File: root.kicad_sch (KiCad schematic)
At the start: 0 parts

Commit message: MCU schematic
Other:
- sheet MCU renamed MCU (page 3)
- added sheet Peripherals (peripherals.kicad_sch)
- sheet MCU (page 3): file MCU.kicad_sch -> MCU_and_EEPROM.kicad_sch
- sheet MCU (page 3) ports: added USB_D_N, USB_D_P; removed none
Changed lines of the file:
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@@
 	(generator_version "10.0")
 	(paper "A4")
+	(wire
+		(pts
+			(xy 82.55 71.12) (xy 100.33 71.12)
+		)
+		(stroke
+			(width 0)
+			(type default)
+		)
+	)
+	(wire
+		(pts
+			(xy 82.55 73.66) (xy 100.33 73.66)
+		)
+		(stroke
+			(width 0)
+			(type default)
+		)
+	)
 	(sheet
 		(at 100.33 58.42)
@@
 			(color 0 0 0 0)
 		)
-		(property "Sheetname" "MCU"
+		(property "Sheetname" "MCU (page 3)"
 			(at 100.33 57.7084 0)
 			(show_name no)
@@
 			)
 		)
-		(property "Sheetfile" "MCU.kicad_sch"
+		(property "Sheetfile" "MCU_and_EEPROM.kicad_sch"
 			(at 100.33 92.0246 0)
 			(show_name no)
@@
 				)
 				(justify left top)
+			)
+		)
+		(pin "USB_D_N" bidirectional
+			(at 100.33 71.12 180)
+			(effects
+				(font
+					(size 1.27 1.27)
+				)
+				(justify left)
+			)
+		)
+		(pin "USB_D_P" bidirectional
+			(at 100.33 73.66 180)
+			(effects
+				(font
+					(size 1.27 1.27)
+				)
+				(justify left)
 			)
 		)
@@
 				)
 			)
+		)
+	)
+	(sheet
+		(at 100.33 19.05)
+		(size 41.91 29.21)
+		(exclude_from_sim no)
+		(in_bom yes)
+		(on_board yes)
+		(dnp no)
+		(fields_autoplaced yes)
+		(stroke
+			(width 0.1524)
+			(type solid)
+		)
+		(fill
+			(color 0 0 0 0)
+		)
+		(property "Sheetname" "Peripherals"
+			(at 100.33 18.3384 0)
+			(show_name no)
+			(do_not_autoplace no)
+			(effects
+				(font
+					(size 1.27 1.27)
+				)
+				(justify left bottom)
+			)
+		)
+		(property "Sheetfile" "peripherals.kicad_sch"
+			(at 100.33 48.8446 0)
+			(show_name no)
+			(do_not_autoplace no)
+			(effects
+				(font
+					(size 1.27 1.27)
+				)
+				(justify left top)
+			)
+		)
+		(instances
+			(project "octo_keyboard"
+				(path "/e2f6b5f5-4c68-42ad-a343-f16c1cb3ab86"
+					(page "6")
+				)
+			)

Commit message: peripherals finished
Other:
- sheet MCU (page 3): file MCU_and_EEPROM.kicad_sch -> MCU.kicad_sch
- sheet MCU (page 3) ports: added COL0, COL1, COL10, COL11, COL12, COL13, COL14, COL2, COL3, COL4, COL5, COL6, COL7, COL8, COL9, EEPROM_SCL, EEPROM_SDA, LED_DATA, ROW0, ROW1, ROW2, ROW3, ROW4, ROW5, SCREEN_CS, SCREEN_DS, SCREEN_SCL, SCREEN_SDA; removed none
- sheet Peripherals ports: added EEPROM_SCL, EEPROM_SDA; removed none

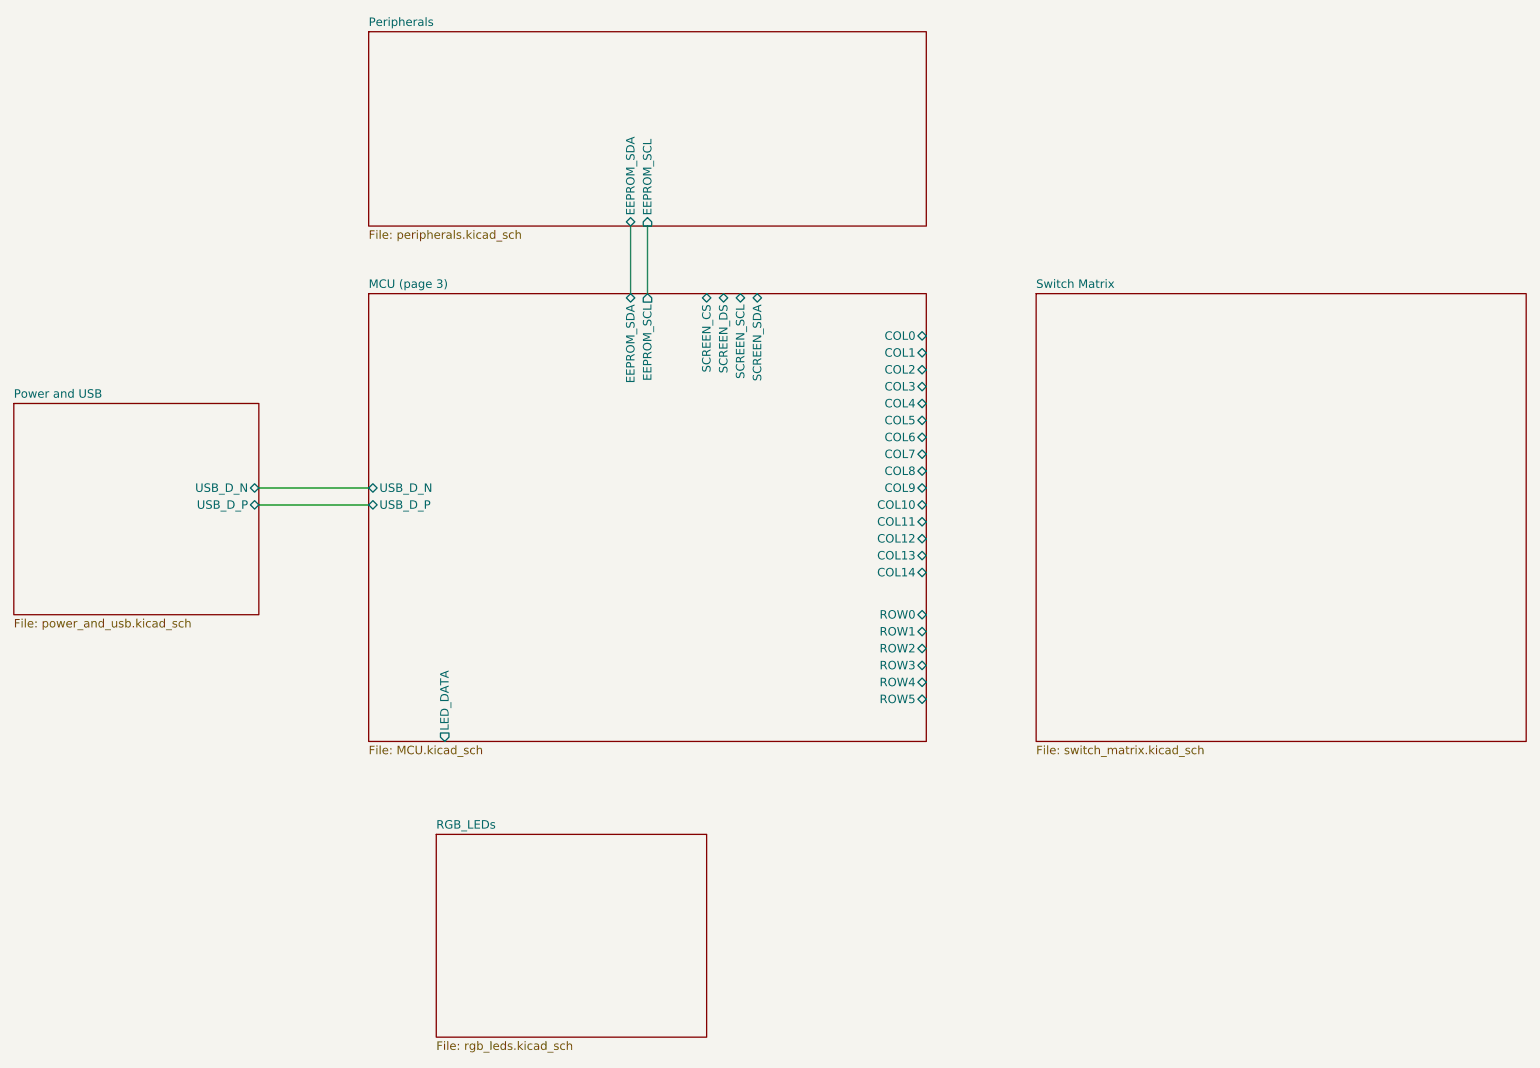
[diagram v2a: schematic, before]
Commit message: cleaned up top-level connections
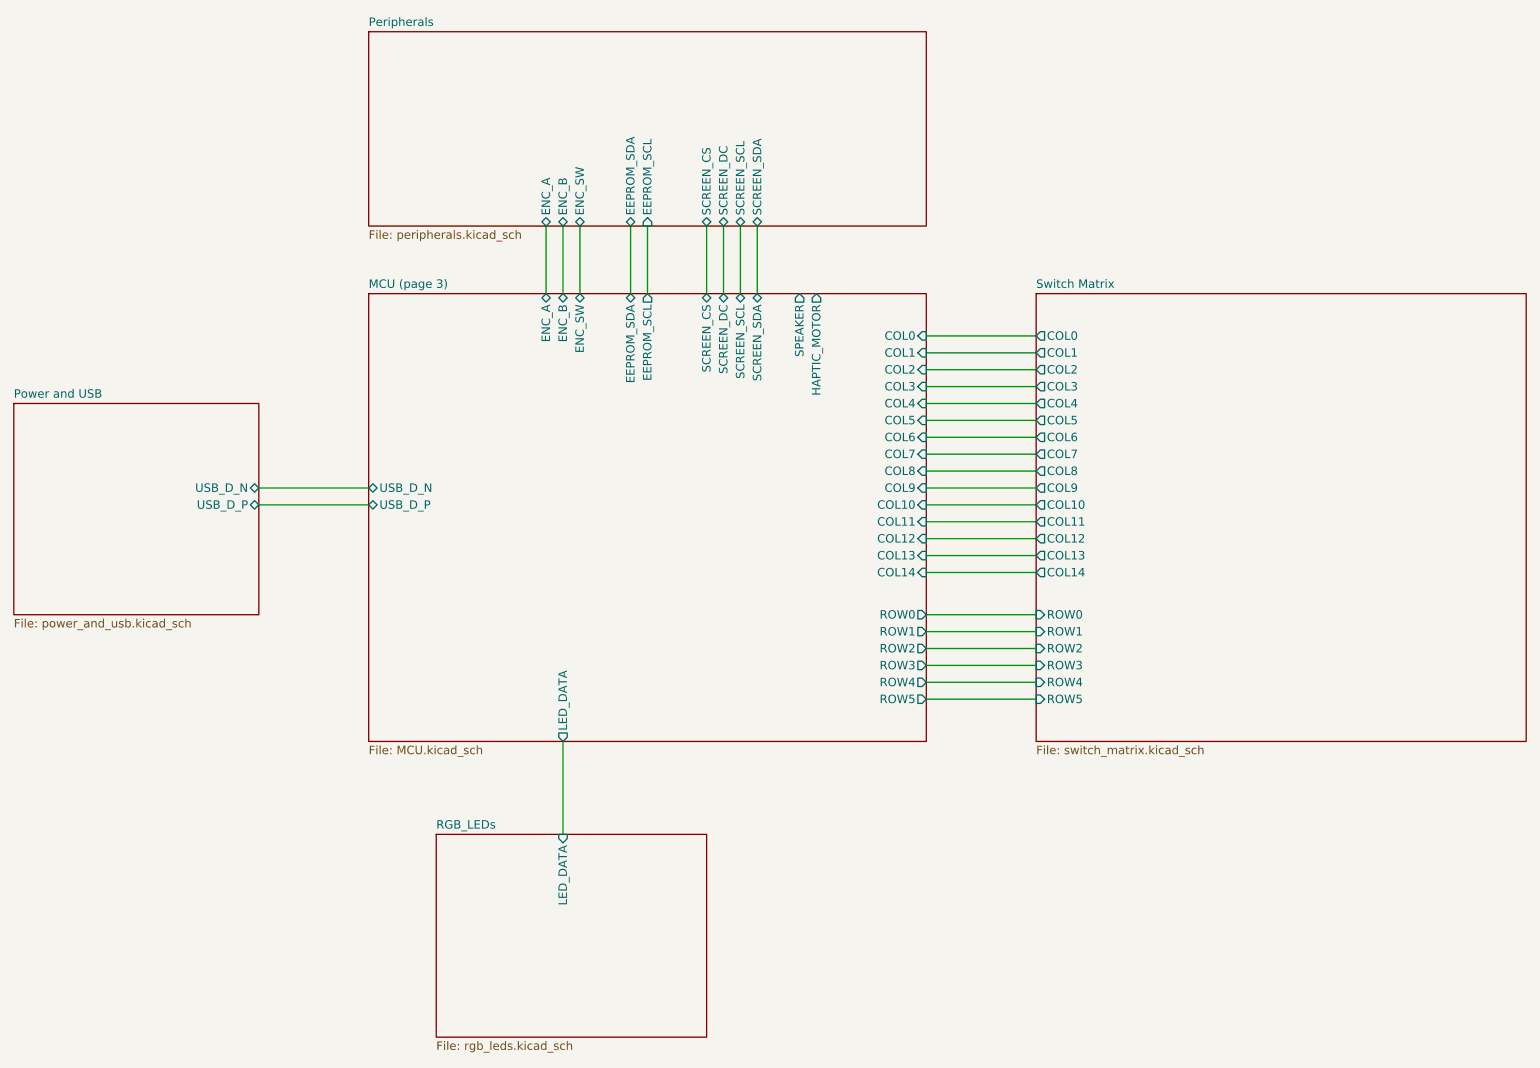
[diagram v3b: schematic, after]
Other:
- sheet MCU (page 3) ports: added ENC_A, ENC_B, ENC_SW, HAPTIC_MOTOR, SCREEN_DC, SPEAKER; removed SCREEN_DS
- sheet Peripherals ports: added ENC_A, ENC_B, ENC_SW, SCREEN_CS, SCREEN_DC, SCREEN_SCL, SCREEN_SDA; removed none
- sheet RGB_LEDs ports: added LED_DATA; removed none
- sheet Switch Matrix ports: added COL0, COL1, COL10, COL11, COL12, COL13, COL14, COL2, COL3, COL4, COL5, COL6, COL7, COL8, COL9, ROW0, ROW1, ROW2, ROW3, ROW4, ROW5; removed none

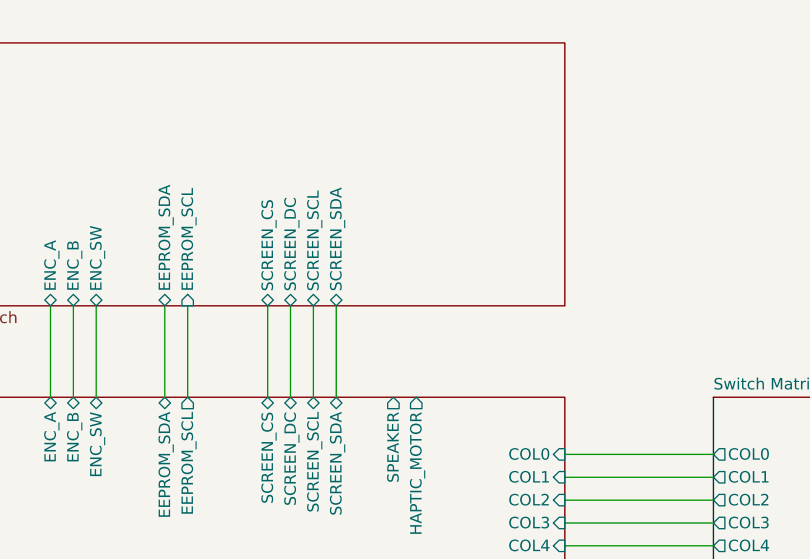
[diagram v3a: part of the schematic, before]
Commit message: documentation for switch matrix, peripherals
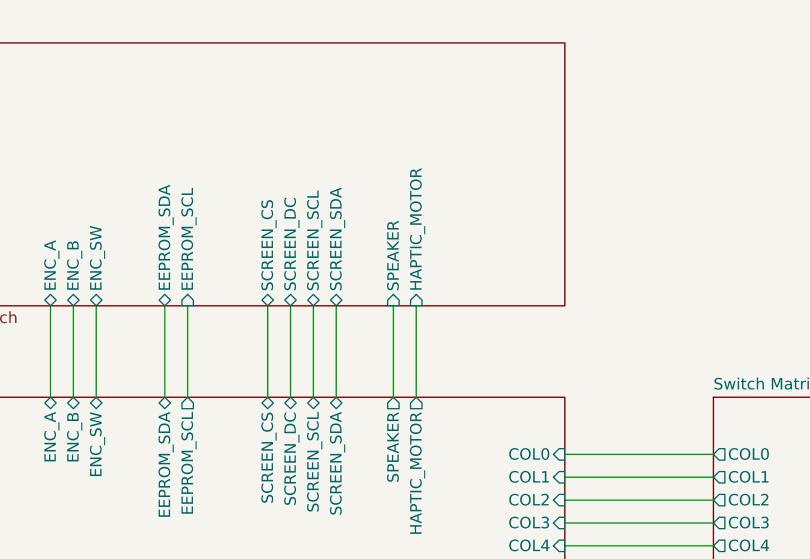
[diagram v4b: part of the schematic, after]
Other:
- sheet Peripherals ports: added HAPTIC_MOTOR, SPEAKER; removed none
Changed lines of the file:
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@@
+	(wire
+		(pts
+			(xy 143.51 46.99) (xy 143.51 57.15)
+		)
+		(stroke
+			(width 0)
+			(type default)
+		)
+	)
 	(wire
 		(pts
@@
 		(pts
 			(xy 162.56 110.49) (xy 179.07 110.49)
+		)
+		(stroke
+			(width 0)
+			(type default)
+		)
+	)
+	(wire
+		(pts
+			(xy 146.05 46.99) (xy 146.05 57.15)
 		)
 		(stroke
@@
 			(effects
 				(font
+					(size 1.27 1.27)
+				)
+				(justify left)
+			)
+		)
+		(pin "HAPTIC_MOTOR" input
+			(at 146.05 46.99 270)
+			(effects
+				(font
+					(size 1.27 1.27)
+				)
+				(justify left)
+			)
+		)
+		(pin "SPEAKER" input
+			(at 143.51 46.99 270)
+			(effects
+				(font
